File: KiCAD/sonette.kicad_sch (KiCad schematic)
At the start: 43 parts, among them J1 STLINK, J2 SERIAL_CON, J3 wav_selector, J4 Conn_01x08_Socket, J5 stlink, Q1 2N3904, Q2 2N3906, SW1 BELL, SW2 RESET, U1 W25Q80DV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

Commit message: écriture de la documentation dans readme.md
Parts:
- removed C14: 10µF/25v, symbol Device:C_Polarized
- removed J1: STLINK, symbol Connector:Conn_01x03_Socket
- added BT1: 3V 2xC, symbol Device:Battery
- added C15: 470µF/16V, symbol Device:C_Polarized
- U4: value LM2937xMP -> LM2937_3.3V
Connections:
- net 3V3: no longer C1.2, C2.1, D1.1 (K), J5.4 (Pin_4), Q2.1 (E), R1.2, R2.1, U1.8 (VCC), U2.8 (VDD), U4.3 (VO)
- net GND: now also C12.2, C13.2, D3.2 (-), U4.2 (GND), BT1.2 (-), C15.2; no longer U3.1 (SHUTDOWN)
- net SWIM: no longer J5.3 (Pin_3)
- net shtdwn: now reaches U2.16 (PB3)
- net shtdwn: now also U3.1 (SHUTDOWN)
- net 3.3V renamed Vdd
- net Vdd: now also C1.2, C2.1, D1.1 (K), J5.3 (Pin_3), J5.4 (Pin_4), Q2.1 (E), R1.2, R2.1, U1.8 (VCC), U2.8 (VDD), C15.1
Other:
- note added: "option 1 alim. piles"
- note added: "option 2 alim. secteur"

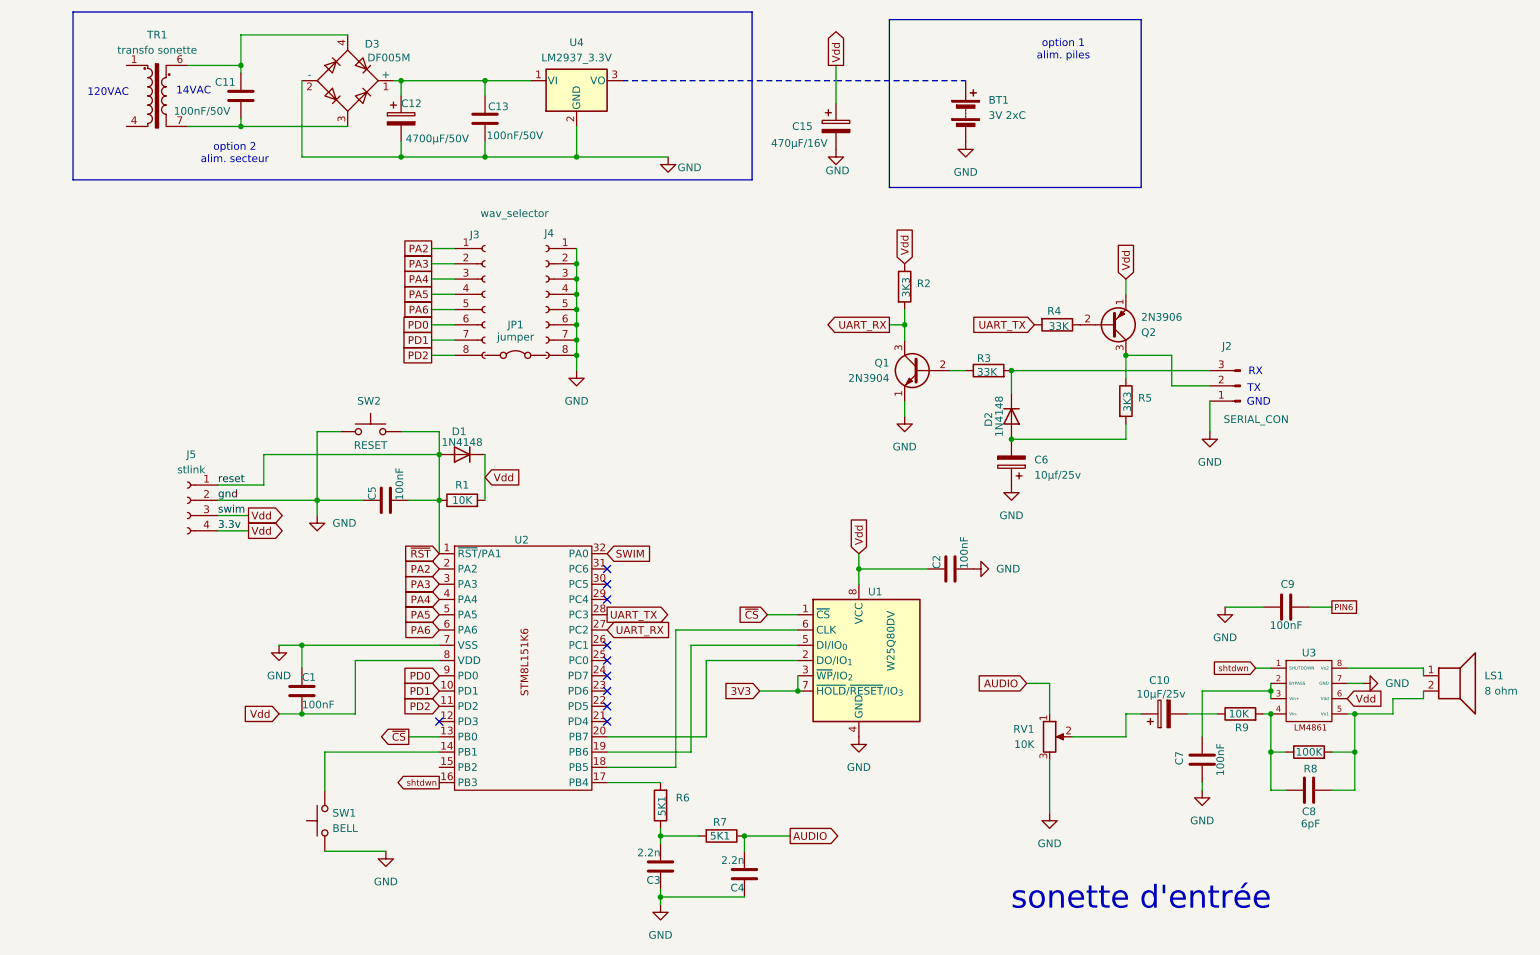
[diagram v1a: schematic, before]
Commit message: Ajouté une LED au circuit qui s'amulle pendant que le WAV est joué. Modifié forth/door-bell.f pour ajouter le contrôle de la LED
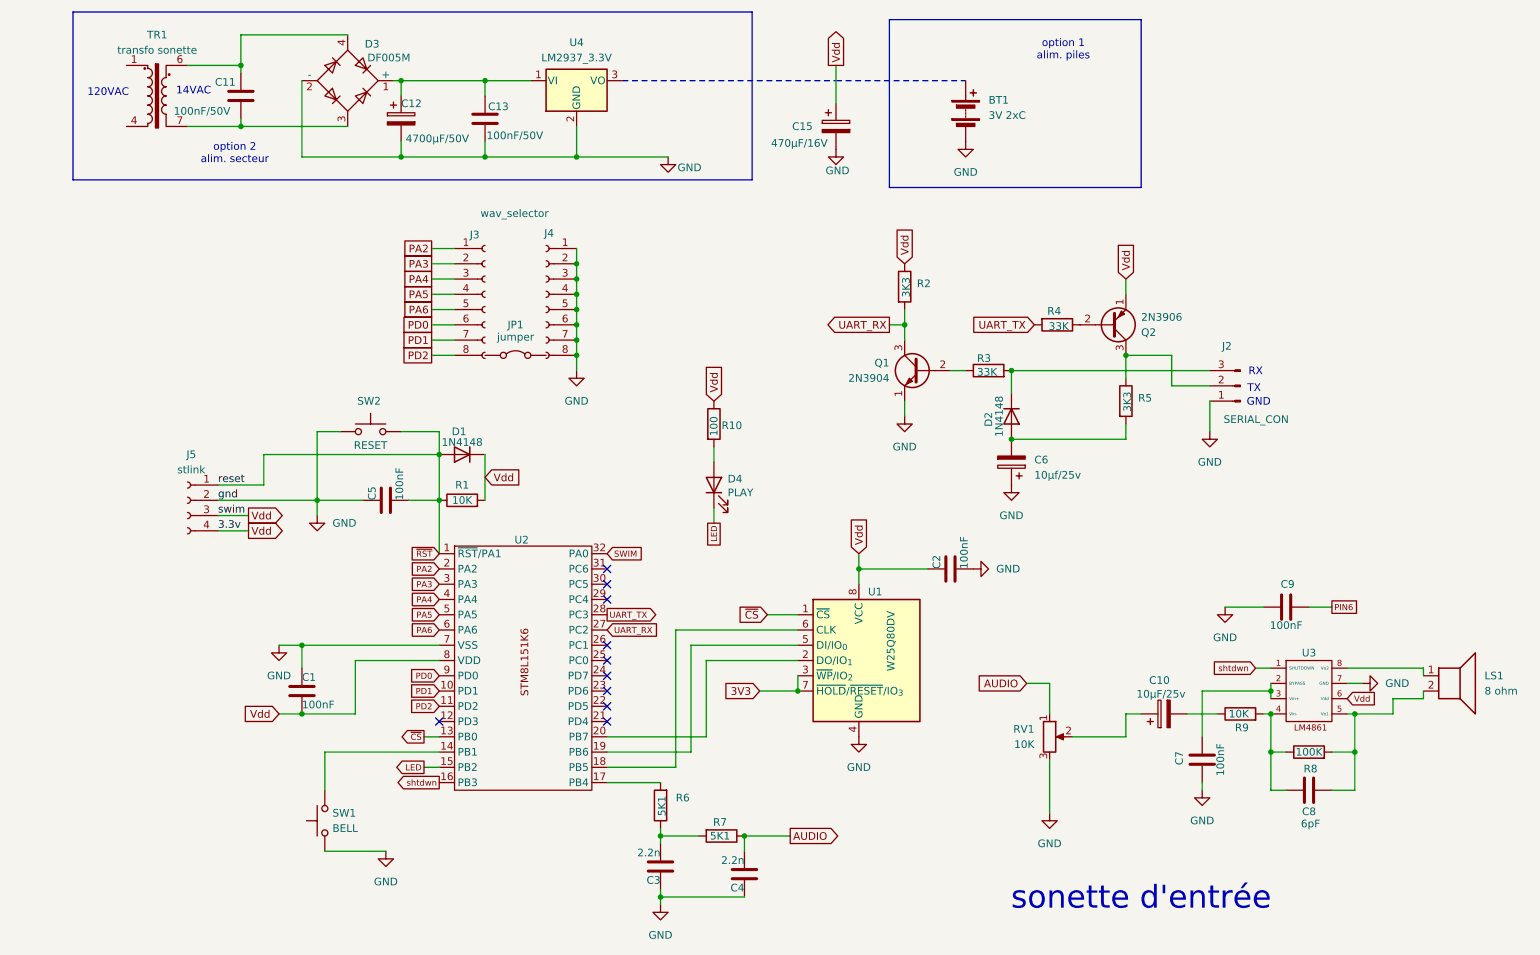
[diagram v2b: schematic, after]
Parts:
- added D4: PLAY, symbol Device:LED
- added R10: 100, symbol Device:R
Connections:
- net Vdd: now also R10.1
- net LED: now reaches U2.15 (PB2)
- net LED: now also D4.1 (K)
- new net: D4.2 (A), R10.2

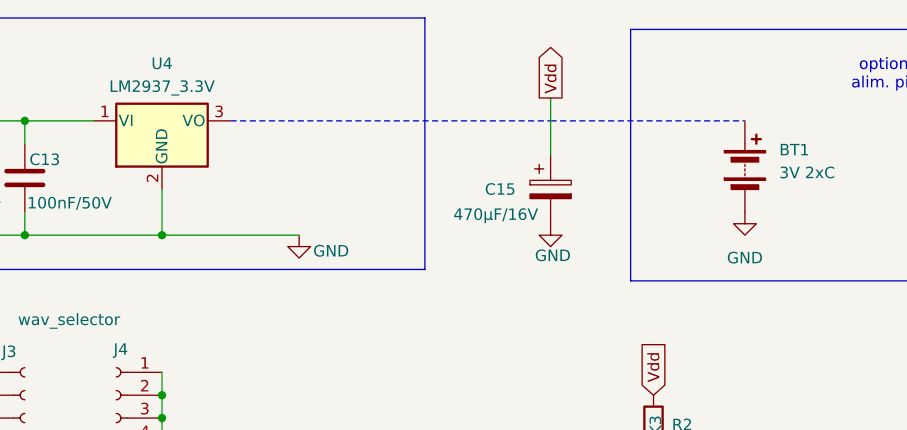
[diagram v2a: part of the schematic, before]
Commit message: Ajout d'un power switch au circuit de l'alimentation secteur
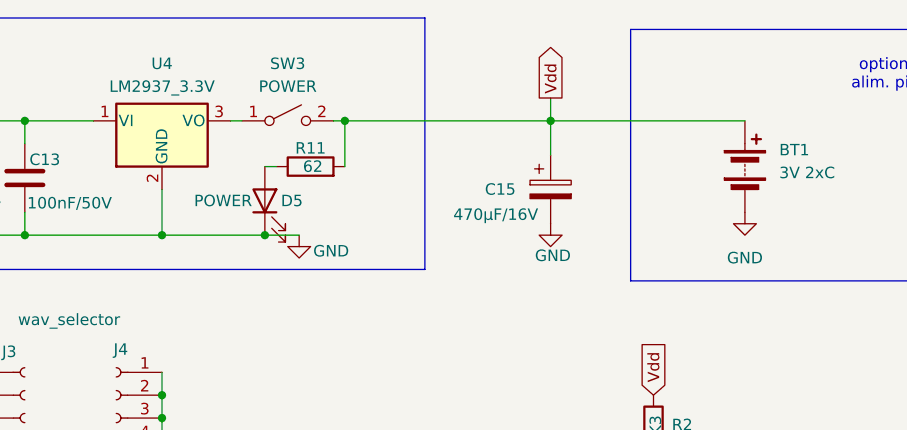
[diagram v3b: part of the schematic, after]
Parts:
- added D5: POWER, symbol Device:LED
- added R11: 62, symbol Device:R
- added SW3: POWER, symbol Switch:SW_SPST
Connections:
- net GND: now also D5.1 (K)
- net Vdd: now also BT1.1 (+), R11.2, SW3.2 (B)
- net at U4.3 (VO): now also SW3.1 (A)
- new net: D5.2 (A), R11.1

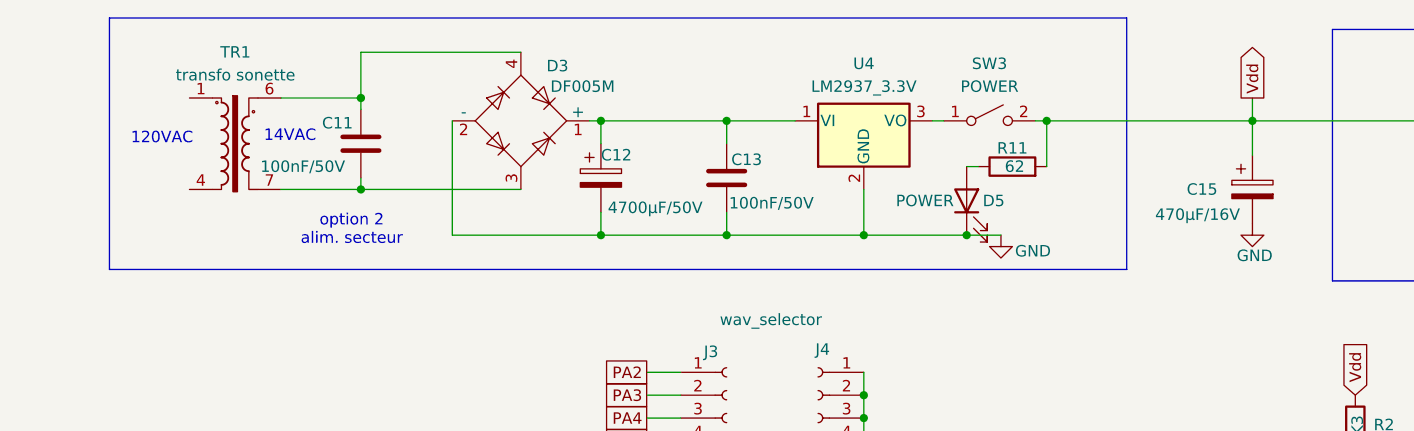
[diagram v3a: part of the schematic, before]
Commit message: Ajout d'un condensateur électrolytique de 47µF à la sortie du régulateur de tension de l'alimentation secteur.
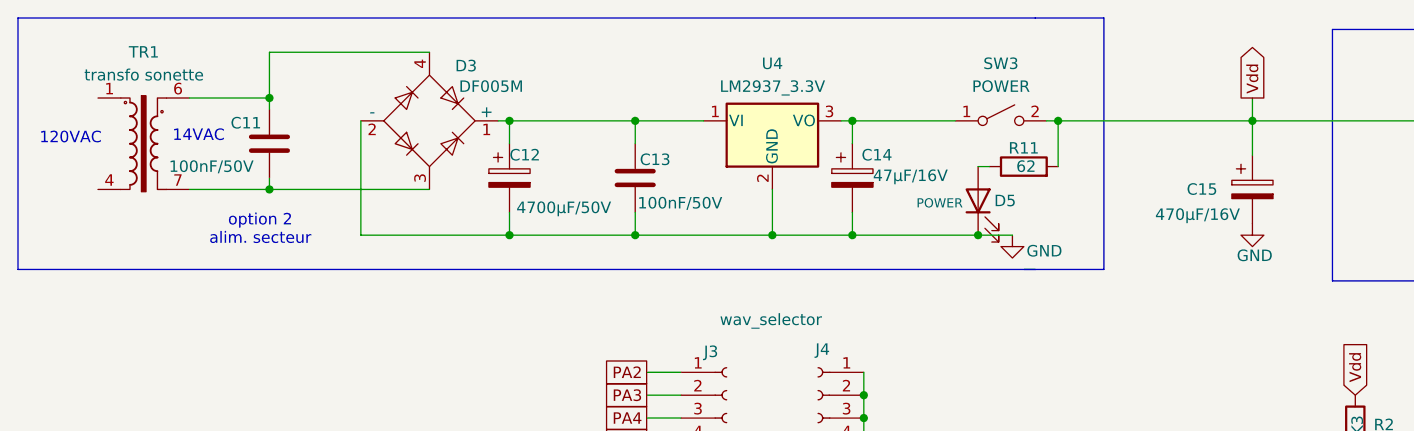
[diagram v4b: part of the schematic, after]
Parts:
- added C14: 47µF/16V, symbol Device:C_Polarized
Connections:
- net GND: now also C14.2
- net at SW3.1 (A), U4.3 (VO): now also C14.1
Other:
- moved on the sheet: C11, C12, C13, D3, D5, R11, SW3, TR1, U4

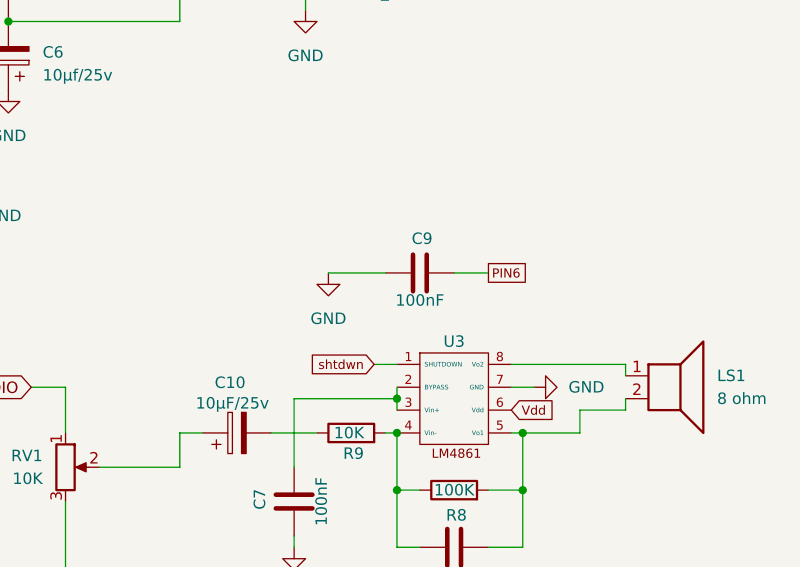
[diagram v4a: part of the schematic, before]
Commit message: Modification à au circuit en ajoutant R12 Modification de door-bell.f pour utilisé le mot DOES>
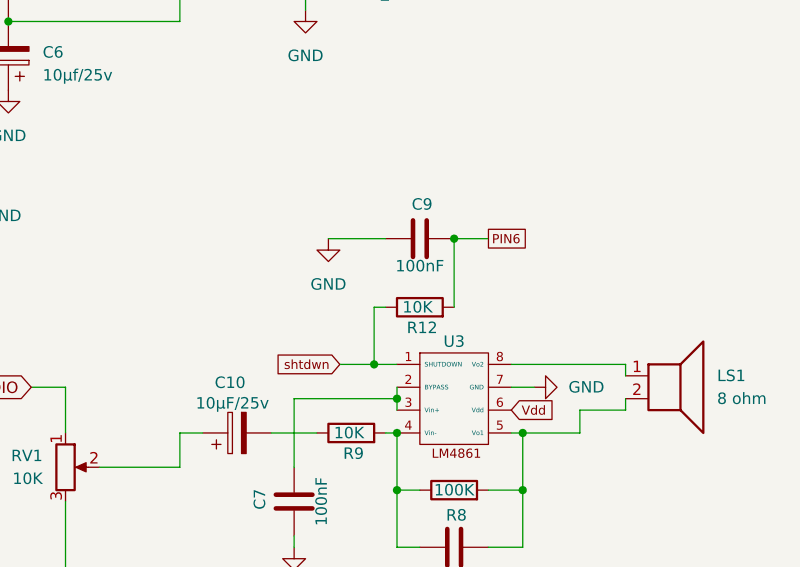
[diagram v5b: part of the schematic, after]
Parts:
- added R12: 10K, symbol Device:R
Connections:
- net PIN6: now also R12.2
- net shtdwn: now also R12.1
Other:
- moved on the sheet: C9
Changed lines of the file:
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@@
 	)
 	(junction
+		(at 233.68 120.65)
+		(diameter 0)
+		(color 0 0 0 0)
+	)
+	(junction
 		(at 101.6 49.53)
 		(diameter 0)
@@
 	)
 	(junction
+		(at 224.79 134.62)
+		(diameter 0)
+		(color 0 0 0 0)
+	)
+	(junction
 		(at 111.76 74.93)
 		(diameter 0)
@@
 	(wire
 		(pts
+			(xy 220.98 134.62) (xy 224.79 134.62)
+		)
+		(stroke
+			(width 0)
+			(type default)
+		)
+	)
+	(wire
+		(pts
 			(xy 128.27 49.53) (xy 124.46 49.53)
 		)
@@
 	(wire
 		(pts
+			(xy 224.79 128.27) (xy 224.79 134.62)
+		)
+		(stroke
+			(width 0)
+			(type default)
+		)
+	)
+	(wire
+		(pts
 			(xy 86.36 46.99) (xy 86.36 49.53)
 		)
@@
 	(wire
 		(pts
-			(xy 233.68 124.46) (xy 237.49 124.46)
+			(xy 233.68 120.65) (xy 237.49 120.65)
 		)
 		(stroke
@@
 	(wire
 		(pts
+			(xy 233.68 120.65) (xy 233.68 128.27)
+		)
+		(stroke
+			(width 0)
+			(type default)
+		)
+	)
+	(wire
+		(pts
 			(xy 111.76 67.31) (xy 111.76 69.85)
 		)
@@
 	(wire
 		(pts
-			(xy 219.71 124.46) (xy 226.06 124.46)
+			(xy 219.71 120.65) (xy 226.06 120.65)
 		)
 		(stroke
@@
 	(wire
 		(pts
+			(xy 226.06 128.27) (xy 224.79 128.27)
+		)
+		(stroke
+			(width 0)
+			(type default)
+		)
+	)
+	(wire
+		(pts
 			(xy 55.88 36.83) (xy 55.88 49.53)
 		)
@@
 	(global_label "PIN6"
 		(shape passive)
-		(at 237.49 124.46 0)
+		(at 237.49 120.65 0)
 		(fields_autoplaced yes)
 		(effects
@@
 		)
 		(property "Intersheetrefs" "${INTERSHEET_REFS}"
-			(at 242.5207 124.46 0)
+			(at 242.5207 120.65 0)
 			(effects
 				(font
@@
 	(global_label "shtdwn"
 		(shape input)
-		(at 224.79 134.62 180)
+		(at 220.98 134.62 180)
 		(fields_autoplaced yes)
 		(effects
@@
 		)
 		(property "Intersheetrefs" "${INTERSHEET_REFS}"
-			(at 217.177 134.62 0)
+			(at 213.367 134.62 0)
 			(effects
 				(font
@@
 	)
 	(symbol
+		(lib_id "Device:R")
+		(at 229.87 128.27 90)
+		(unit 1)
+		(exclude_from_sim no)
+		(in_bom yes)
+		(on_board yes)
+		(dnp no)
+		(property "Reference" "R12"
+			(at 230.124 130.556 90)
+			(effects
+				(font
+					(size 1.27 1.27)
+				)
+			)
+		)
+		(property "Value" "10K"
+			(at 229.616 128.27 90)
+			(effects
+				(font
+					(size 1.27 1.27)
+				)
+			)
+		)
+		(property "Footprint" ""
+			(at 229.87 130.048 90)
+			(effects
+				(font
+					(size 1.27 1.27)
+				)
+				(hide yes)
+			)
+		)
+		(property "Datasheet" "~"
+			(at 229.87 128.27 0)
+			(effects
+				(font
+					(size 1.27 1.27)
+				)
+				(hide yes)
+			)
+		)
+		(property "Description" "Resistor"
+			(at 229.87 128.27 0)
+			(effects
+				(font
+					(size 1.27 1.27)
+				)
+				(hide yes)
+			)
+		)
+		(pin "1"
+		)
+		(pin "2"
+		)
+		(instances
+			(project "sonette"
+				(path "/f9fee92e-b526-4b75-96ae-352cd94e2ffe"
+					(reference "R12")
+					(unit 1)
+				)
+			)
+		)
+	)
+	(symbol
 		(lib_id "Connector:Conn_01x04_Socket")
 		(at 46.99 106.68 0)
@@
 	(symbol
 		(lib_id "power:GND")
-		(at 219.71 124.46 0)
+		(at 219.71 120.65 0)
 		(unit 1)
 		(exclude_from_sim no)
@@
 		(dnp no)
 		(property "Reference" "#PWR011"
-			(at 219.71 130.81 0)
+			(at 219.71 127 0)
 			(effects
 				(font
@@
 		)
 		(property "Value" "GND"
-			(at 219.71 129.54 0)
+			(at 219.71 125.73 0)
 			(effects
 				(font
@@
 		)
 		(property "Footprint" ""
-			(at 219.71 124.46 0)
+			(at 219.71 120.65 0)
 			(effects
 				(font
@@
 		)
 		(property "Datasheet" ""
-			(at 219.71 124.46 0)
+			(at 219.71 120.65 0)
 			(effects
 				(font
@@
 		)
 		(property "Description" "Power symbol creates a global label with name \"GND\" , ground"
-			(at 219.71 124.46 0)
+			(at 219.71 120.65 0)
 			(effects
 				(font
@@
 	(symbol
 		(lib_id "Device:C")
-		(at 229.87 124.46 90)
+		(at 229.87 120.65 90)
 		(unit 1)
 		(exclude_from_sim no)
@@
 		(dnp no)
 		(property "Reference" "C9"
-			(at 230.124 120.65 90)
+			(at 230.124 116.84 90)
 			(effects
 				(font
@@
 		)
 		(property "Value" "100nF"
-			(at 229.87 127.508 90)
+			(at 229.87 123.698 90)
 			(effects
 				(font
@@
 		)
 		(property "Footprint" ""
-			(at 233.68 123.4948 0)
+			(at 233.68 119.6848 0)
 			(effects
 				(font
@@
 		)
 		(property "Datasheet" "~"
-			(at 229.87 124.46 0)
+			(at 229.87 120.65 0)
 			(effects
 				(font
@@
 		)
 		(property "Description" "Unpolarized capacitor"
-			(at 229.87 124.46 0)
+			(at 229.87 120.65 0)
 			(effects
 				(font
